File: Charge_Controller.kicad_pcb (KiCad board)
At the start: 2 copper layers, 134.6 x 76.2 mm, 159 parts, among them J1 SOLAR, J10 Conn_01x01_Female, J11 Conn_01x01_Female, J12 Conn_01x01_Female, J13 Conn_01x01_Female, J14 Conn_01x01_Female, J15 Conn_01x01_Female, J16 Conn_01x01_Female, J17 Conn_01x01_Female, J18 Conn_01x01_Female, J19 Conn_01x01_Female, J2 Conn_01x01_Female, J20 Conn_01x01_Female, J21 Conn_01x01_Female, J22 Conn_01x01_Female, J23 Conn_01x01_Female, J24 Conn_01x01_Female, J25 Conn_01x01_Female, J26 Conn_01x01_Female, J27 Conn_01x01_Female, J28 Conn_01x01_Female, J29 Conn_01x01_Female, J3 Conn_01x01_Female, J30 Conn_01x01_Female, J31 Conn_01x01_Female, J32 Conn_01x01_Female, J33 Conn_01x01_Female, J34 Conn_01x01_Female, J36 FAN, J38 I2C_CON, J4 Conn_01x01_Female, J5 Conn_01x01_Female, J6 Conn_01x01_Female, J7 Conn_01x01_Female, J8 BATT, J9 USB_OTG, Q1 CSD19505, Q2 CSD19505, Q3 CSD19505, Q4 Si2306, Q5 2N3904, Q6 2N3904, Q7 PMOS-100V-78A, Q8 PMOS-100V-78A, Q9 Si2306, SW1 RIGHT, SW2 LEFT, SW3 BACK, SW4 SELECT, U1 ACS712-30A, U10 ADS1015, U11 NUP4202, U12 PCF8574, U2 B1212, U3 AMS1117-5.0, U4 AMS1117-3.3, U5 XL7005A, U6 XL7005A, U7 IR2104, U8 ESP32-WROOM-32, U9 CH340C

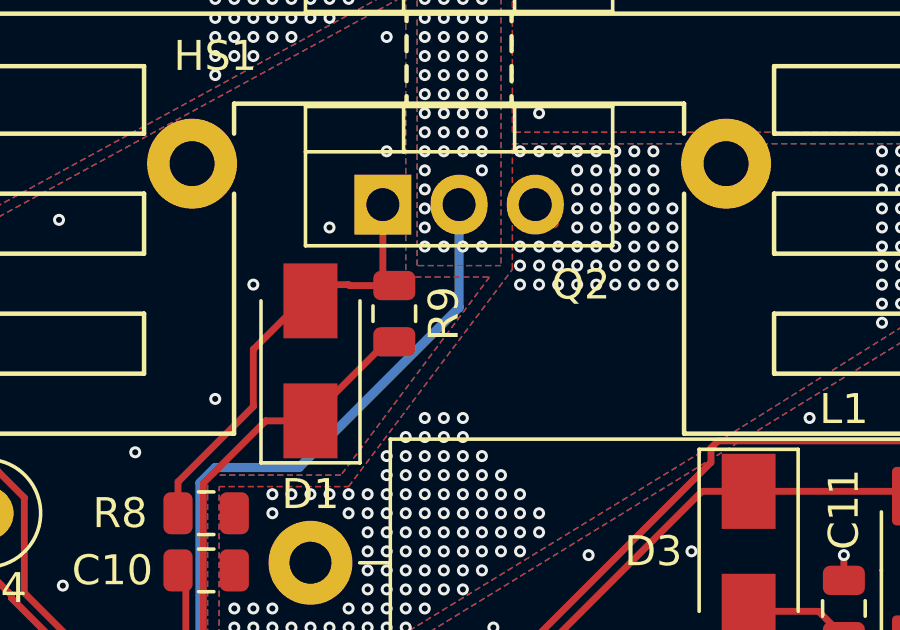
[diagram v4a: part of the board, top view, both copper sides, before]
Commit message: Changed the hall sensor and added some notes.
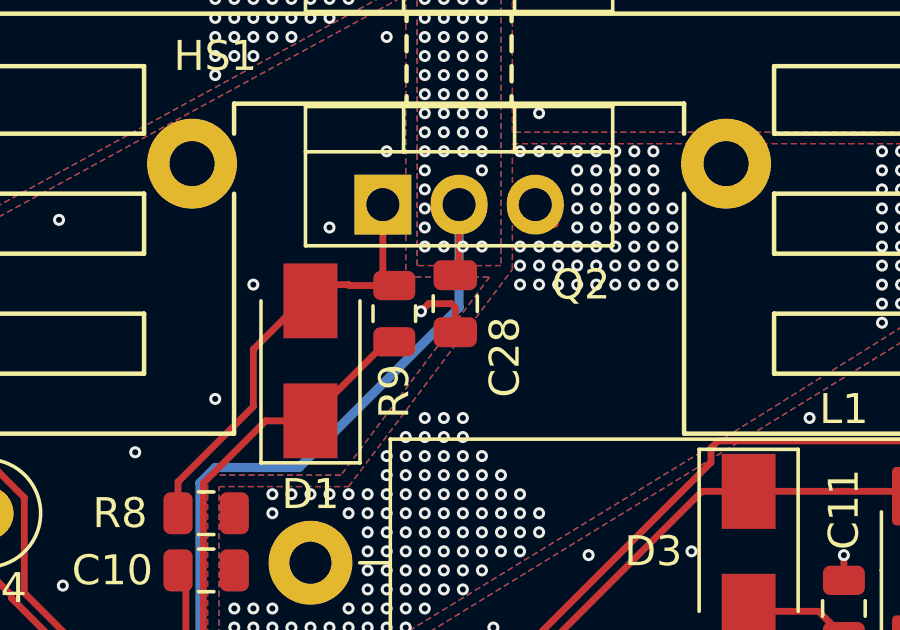
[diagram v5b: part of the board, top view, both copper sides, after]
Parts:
- added C28: 100nf, Capacitor_SMD:C_0805_2012Metric, F.Cu at (151.3, 83.5)
- U1: value ACS712-30A -> Hall Amp Sense
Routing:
- net /S+Fused3: track 38.5 -> 40.9 mm
- net GND: track 129.4 -> 131.5 mm, vias 764 -> 765
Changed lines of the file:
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@@
     (property "Sheetname" "")
     (attr smd)
-    (fp_text reference "R9" (at 0 1.651 90) (layer "F.SilkS")
+    (fp_text reference "R9" (at -2.5885 0 90) (layer "F.SilkS")
       (effects (font (size 1 1) (thickness 0.15)))
     )
@@
     (descr "SOIC, 8 Pin (JEDEC MS-012AA, https://www.analog.com/media/en/package-pcb-resources/package/pkg_pdf/soic_narrow-r/r_8.pdf), generated with kicad-footprint-generator ipc_gullwing_generator.py")
     (tags "SOIC SO")
-    (property "LCSC" "C9932")
+    (property "LCSC" "C2930869")
     (property "Sheetfile" "Charge_Controller.kicad_sch")
     (property "Sheetname" "")
@@
       (effects (font (size 1 1) (thickness 0.15)))
     )
-    (fp_text value "ACS712-30A" (at 3.4 0 180) (layer "F.Fab")
+    (fp_text value "Hall Amp Sense" (at 3.4 0 180) (layer "F.Fab")
       (effects (font (size 1 1) (thickness 0.15)))
     )
@@
     )
   )
+  (footprint "Capacitor_SMD:C_0805_2012Metric" (layer "F.Cu")
+    (at 151.286 83.49 90)
+    (descr "Capacitor SMD 0805 (2012 Metric), square (rectangular) end terminal, IPC_7351 nominal, (Body size source: IPC-SM-782 page 76, https://www.pcb-3d.com/wordpress/wp-content/uploads/ipc-sm-782a_amendment_1_and_2.pdf, https://docs.google.com/spreadsheets/d/1BsfQQcO9C6DZCsRaXUlFlo91Tg2WpOkGARC1WS5S8t0/edit?usp=sharing), generated with kicad-footprint-generator")
+    (tags "capacitor")
+    (property "Field4" "16v")
+    (property "LCSC" "C28233")
+    (property "Sheetfile" "Charge_Controller.kicad_sch")
+    (property "Sheetname" "")
+    (attr smd)
+    (fp_text reference "C28" (at -1.778 1.651 90) (layer "F.SilkS")
+      (effects (font (size 1 1) (thickness 0.15)))
+    )
+    (fp_text value "100nf" (at 0 1.68 90) (layer "F.Fab")
+      (effects (font (size 1 1) (thickness 0.15)))
+    )
+    (fp_text user "${REFERENCE}" (at 0 0 90) (layer "F.Fab")
+      (effects (font (size 0.5 0.5) (thickness 0.08)))
+    )
+    (fp_line (start -0.261252 -0.735) (end 0.261252 -0.735) (layer "F.SilkS") (width 0.12))
+    (fp_line (start -0.261252 0.735) (end 0.261252 0.735) (layer "F.SilkS") (width 0.12))
+    (fp_line (start 1.7 -0.98) (end 1.7 0.98) (layer "F.CrtYd") (width 0.05))
+    (fp_line (start -1.7 0.98) (end -1.7 -0.98) (layer "F.CrtYd") (width 0.05))
+    (fp_line (start 1.7 0.98) (end -1.7 0.98) (layer "F.CrtYd") (width 0.05))
+    (fp_line (start -1.7 -0.98) (end 1.7 -0.98) (layer "F.CrtYd") (width 0.05))
+    (fp_line (start 1 -0.625) (end 1 0.625) (layer "F.Fab") (width 0.1))
+    (fp_line (start -1 0.625) (end -1 -0.625) (layer "F.Fab") (width 0.1))
+    (fp_line (start -1 -0.625) (end 1 -0.625) (layer "F.Fab") (width 0.1))
+    (fp_line (start 1 0.625) (end -1 0.625) (layer "F.Fab") (width 0.1))
+    (pad "1" smd roundrect (at -0.95 0 90) (size 1 1.45) (layers "F.Cu" "F.Paste" "F.Mask") (roundrect_rratio 0.25)
+      (net 1 "GND") (pintype "passive"))
+    (pad "2" smd roundrect (at 0.95 0 90) (size 1 1.45) (layers "F.Cu" "F.Paste" "F.Mask") (roundrect_rratio 0.25)
+      (net 87 "/S+Fused3") (pintype "passive"))
+    (model "${KICAD6_3DMODEL_DIR}/Capacitor_SMD.3dshapes/C_0805_2012Metric.wrl"
+      (offset (xyz 0 0 0))
+      (scale (xyz 1 1 1))
+      (rotate (xyz 0 0 0))
+    )
+  )
   (footprint "Diode_SMD:D_SMC-RM10_Universal_Handsoldering" (layer "F.Cu")
     (at 89.691 81.585 180)
@@
   (segment (start 145.19 125.9375) (end 145.19 127.051) (width 0.2286) (layer "F.Cu") (net 1))
   (segment (start 180.115 143.2285) (end 179.1475 143.2285) (width 0.2286) (layer "F.Cu") (net 1))
+  (segment (start 151.159 83.49) (end 150.397 83.49) (width 0.2286) (layer "F.Cu") (net 1))
   (segment (start 118.455 111.665) (end 118.455 110.395) (width 0.2286) (layer "F.Cu") (net 1))
   (segment (start 170.398 94.855) (end 170.717 95.174) (width 0.2286) (layer "F.Cu") (net 1))
@@
   (segment (start 181.796 142.515) (end 182.02 142.515) (width 0.2286) (layer "F.Cu") (net 1))
   (segment (start 160.185 142.78) (end 158.544 142.78) (width 0.2286) (layer "F.Cu") (net 1))
+  (segment (start 151.286 84.44) (end 151.286 83.617) (width 0.2286) (layer "F.Cu") (net 1))
   (segment (start 113.501 133.335) (end 113.44 133.335) (width 0.2286) (layer "F.Cu") (net 1))
   (segment (start 147.73 126.67) (end 147.349 127.051) (width 0.2286) (layer "F.Cu") (net 1))
   (segment (start 120.985 118.086) (end 120.933 118.034) (width 0.2286) (layer "F.Cu") (net 1))
+  (segment (start 150.397 83.49) (end 150.143 83.744) (width 0.2286) (layer "F.Cu") (net 1))
   (segment (start 141.99 127.3) (end 144.941 127.3) (width 0.2286) (layer "F.Cu") (net 1))
   (segment (start 75.975 113.89) (end 75.975 113.3038) (width 0.2286) (layer "F.Cu") (net 1))
@@
   (segment (start 128.426 85.649) (end 128.3475 85.649) (width 0.2286) (layer "F.Cu") (net 1))
   (segment (start 85.616 123.125) (end 84.484 124.257) (width 0.2286) (layer "F.Cu") (net 1))
+  (segment (start 151.286 83.617) (end 151.159 83.49) (width 0.2286) (layer "F.Cu") (net 1))
   (segment (start 123.843 83.12) (end 124.78358 82.17942) (width 0.2286) (layer "F.Cu") (net 1))
   (segment (start 128.445 86.9) (end 128.426 86.919) (width 0.2286) (layer "F.Cu") (net 1))
@@
   (via (at 71.53 80.315) (size 0.4) (drill 0.2) (layers "F.Cu" "B.Cu") (free) (net 1))
   (via (at 114.71 130.48) (size 0.4) (drill 0.2) (layers "F.Cu" "B.Cu") (free) (net 1))
+  (via (at 150.143 83.744) (size 0.4) (drill 0.2) (layers "F.Cu" "B.Cu") (net 1))
   (via (at 74.07 77.14) (size 0.4) (drill 0.2) (layers "F.Cu" "B.Cu") (free) (net 1))
   (via (at 177.575 112.065) (size 0.4) (drill 0.2) (layers "F.Cu" "B.Cu") (free) (net 1))
@@
   (via (at 190.91 80.95) (size 0.4) (drill 0.2) (layers "F.Cu" "B.Cu") (free) (net 86))
   (segment (start 150.397 96.582041) (end 153.191 99.376041) (width 0.3048) (layer "F.Cu") (net 87))
+  (segment (start 151.286 82.54) (end 151.413 82.413) (width 0.2286) (layer "F.Cu") (net 87))
+  (segment (start 151.413 82.413) (end 151.413 80.188) (width 0.2286) (layer "F.Cu") (net 87))
   (segment (start 153.191 99.376041) (end 153.191 105.715) (width 0.3048) (layer "F.Cu") (net 87))
   (via (at 151.54 71.425) (size 0.4) (drill 0.2) (layers "F.Cu" "B.Cu") (net 87))

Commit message: Draft layout, still needs a bunch, but everything is connected.
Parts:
- added H1: Holder, Fuse_Holder:Fuse_Blade_C2935871, F.Cu at (79.7, 69.1)
- added H2: Holder, Fuse_Holder:Fuse_Blade_C2935871, F.Cu at (199.1, 68.2)
- added L11: 7443783533650, 7443783533650_inductor:7443783533650, F.Cu at (158.3, 79.0)
- C28: value 100nf -> 470nf
- F1, F2: value 35A -> 25A; footprint Fuse:Fuseholder_Blade_Mini_Keystone_3568 -> Symbol:ESD-Logo_6.6x6mm_SilkScreen; moved to B.Cu
- HS1: value Heatsink -> 100x41x8mm Aluminum Heat Sink; footprint Heatsink:Heatsink_Stonecold_HS-132_32x14mm_2xFixation1.5mm -> MountingHole:MountingHole_2.5mm_Pad_Via; moved to B.Cu
- J1, J36, J8: footprint Phoenix_10.16_terminal_1709681:Phoenix_10.16_terminal_1709681 -> TerminalBlock_MetzConnect:TerminalBlock_MetzConnect_Type703_RT10N02HGLU_1x02_P9.52mm_Horizontal
- J33, J34: footprint TestPoint:TestPoint_Loop_D3.50mm_Drill0.9mm_Beaded -> MountingHole:MountingHole_2.5mm_Pad_Via
- Q1, Q2, Q3: footprint Package_TO_SOT_THT:TO-220-3_Vertical -> Package_TO_SOT_SMD:TO-263-2
- moved F2 117.5 mm to (84.6, 73.3)
- moved F1 108.5 mm to (194.5, 74.0), turned to 180 degrees
- moved J5 54.0 mm to (189.4, 122.9)
- moved J33 52.8 mm to (194.4, 124.4)
- moved LOGO1 43.4 mm to (155.7, 111.4)
- moved HS1 41.6 mm to (110.0, 82.5), turned to 180 degrees
- moved J8 41.0 mm to (202.2, 122.9), turned to 90 degrees
- moved R37 40.9 mm to (103.6, 71.1)
- moved R13 40.1 mm to (133.8, 96.3), turned to 0 degrees
- moved C7 39.6 mm to (120.3, 83.7), turned to -90 degrees
- moved R11 38.8 mm to (143.3, 90.7)
- moved Q1 38.6 mm to (112.9, 72.9), turned to 0 degrees
- moved R10 37.7 mm to (141.4, 94.8), turned to 0 degrees
- moved R6 37.2 mm to (104.5, 67.9), turned to 180 degrees
- moved D2 35.5 mm to (139.9, 90.2)
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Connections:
- net Net-(LED2-Pad2) renamed /L2
- C16 pad 1: /3.3V -> +3.3VA
- C17 pad 1: /3.3V -> +3.3VA
- HS1 pad 1: (no net) -> GND
- J3 pad 1: /3.3V -> +3.3VA
- J36 pad 1: /12V -> Net-(Q9-Pad1)
- J36 pad 2: Net-(J36-Pad2) -> /12V
- J8 pad 1: /B+ -> GND
- J8 pad 2: GND -> /B+
- L3 pad 2: /3.3V -> +3.3VA
- Q9 pad 1: Net-(J36-Pad2) -> Net-(Q9-Pad1)
- R17 pad 1: /3.3V -> +3.3VA
- R18 pad 1: /3.3V -> +3.3VA
- U1 pad 1: /S+Polarity -> /S+Fused2
- U1 pad 2: /S+Polarity -> /S+Fused2
- U1 pad 3: /S+Fused2 -> /S+Polarity
- U1 pad 4: /S+Fused2 -> /S+Polarity
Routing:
- net /S+B+1A: track 172.1 -> 112.1 mm
- net /12V: track 161.5 -> 214.5 mm
- net /S+Polarity: track 0.00 -> 39.6 mm, vias 99 -> 17
- net +3.3VA: track 398.5 -> 437.7 mm
- net Net-(D1-Pad1): track 42.4 -> 9.58 mm
- net Net-(C4-Pad2): track 40.1 -> 72.6 mm, vias 1 -> 0
- net /GPIO32: track 67.5 -> 98.3 mm
- net /GPIO33: track 70.4 -> 97.7 mm
- net Net-(J36-Pad2): track 26.7 -> 0.00 mm
- net Net-(C3-Pad1): track 75.0 -> 48.8 mm, vias 2 -> 0
- net /S+Fused3: track 40.9 -> 14.8 mm, vias 64 -> 0
- net Net-(C10-Pad1): track 29.1 -> 5.92 mm
- net /B+Fused: track 41.2 -> 63.5 mm, vias 200 -> 0
- net GND: track 131.5 -> 152.6 mm, vias 765 -> 198
- net /SDA: track 124.8 -> 145.8 mm
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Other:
- board size 134.6 x 76.2 mm -> 139.7 x 88.9 mm
- board text added: "heat sink"
- board text removed: "BAT"
